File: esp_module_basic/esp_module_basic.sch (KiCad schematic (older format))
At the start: 19 parts, among them P1 CONN_01X4, P2 CONN_01X15, P3 CONN_01X15

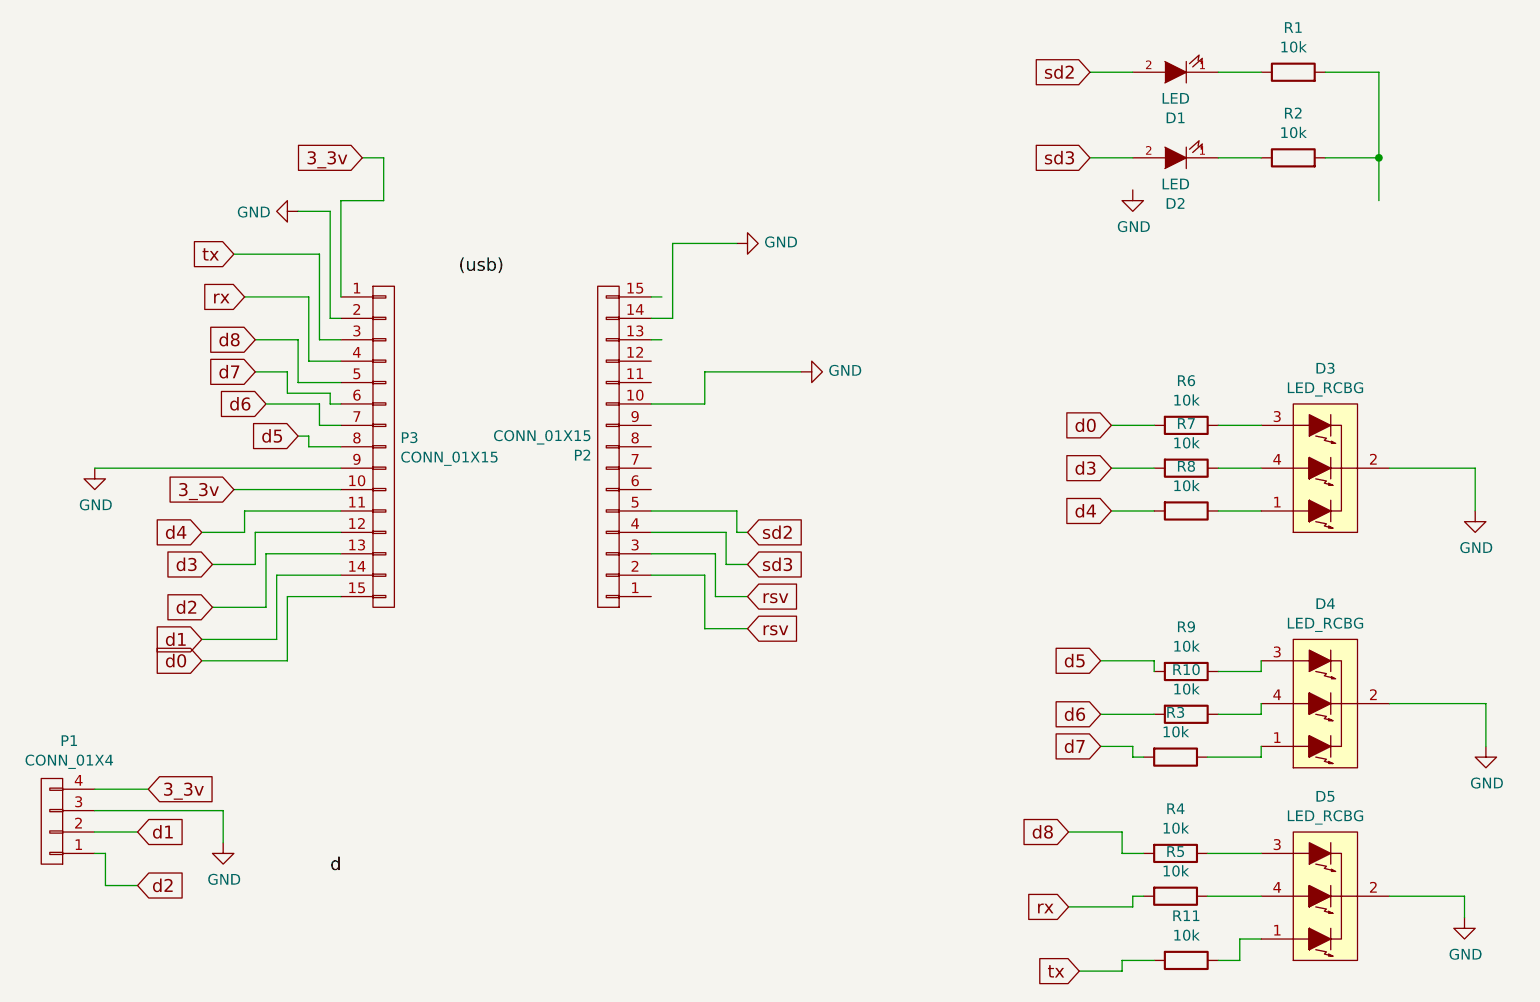
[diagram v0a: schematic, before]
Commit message: fix ground connection and fix labels for shared unconnected pins
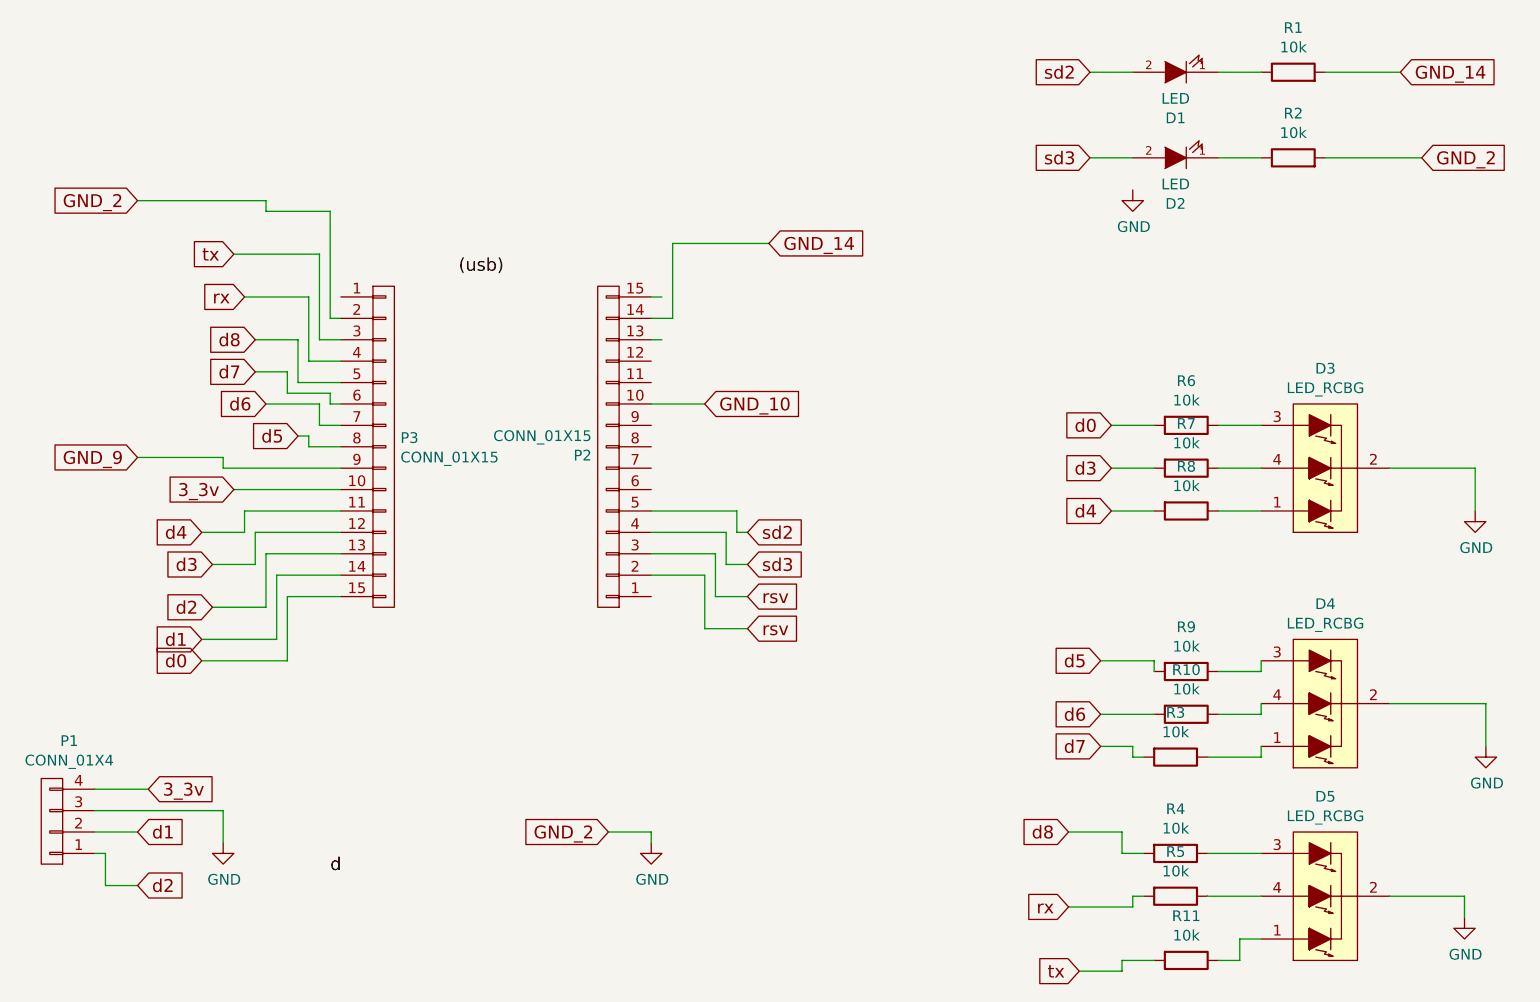
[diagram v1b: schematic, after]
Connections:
- net 3_3v: no longer P3.1 (P1)
- net GND: now also R2.2; no longer P2.10 (P10), P2.14 (P14), P3.9 (P9)
- net GND_14: now reaches R1.2
- net GND_14: now also P2.14 (P14); no longer R2.2
- new net GND_10: P2.10 (P10)
- new net GND_9: P3.9 (P9)
